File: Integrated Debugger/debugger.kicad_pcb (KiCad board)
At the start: 4 copper layers, 36.8 x 16.4 mm, 49 parts, among them J1 B2B GT-B0353FSV06-08B0201, J2 USB_C (PC <-> Host), J3 FPC socket 10P, J4 20021521-00010T1LF, J5 PWR, Q1 NMOS DMN2991UDA-7B, Q2 PMOS DMP32D9UDA-7B, SW1 RESET, SW2 BOOT, U1 TPS7A2633DRVR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

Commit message: feat: wip board layout and routing
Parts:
- C10, C11: moved to B.Cu
- D6, Q1, Q2, U1, U8: moved to F.Cu
- moved D6 65.4 mm to (104.4, 94.8), turned to -90 degrees
- moved Q2 63.2 mm to (105.9, 92.8)
- moved J1 62.8 mm to (129.9, 88.5), turned to 90 degrees
- moved U8 61.5 mm to (106.0, 95.2), turned to 0 degrees
- moved U1 56.8 mm to (123.0, 83.8), turned to -90 degrees
- moved R13 56.8 mm to (112.1, 94.1), turned to 90 degrees
- moved R14 54.4 mm to (113.2, 93.8)
- moved R15 53.5 mm to (113.2, 94.5), turned to 180 degrees
- moved C8 50.9 mm to (112.7, 84.3), turned to -90 degrees
- moved C3 48.9 mm to (120.6, 86.6), turned to 90 degrees
- moved R17 48.1 mm to (106.2, 91.6)
- moved C9 47.1 mm to (119.1, 85.0)
- moved R16 41.4 mm to (109.8, 83.9), turned to -90 degrees
- moved C10 32.4 mm to (110.0, 91.0)
- moved C13 31.3 mm to (108.6, 94.4)
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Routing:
- net V_TARGET: track 5.86 -> 29.8 mm, vias 1 -> 3
- net /MCU/~{RST}: track 0.00 -> 16.9 mm, vias 0 -> 2
- net /MCU/TARGET_EN: track 0.00 -> 15.2 mm, vias 0 -> 3
- net /MCU/SWD.IO: track 1.07 -> 15.4 mm
- net +5V: track 4.33 -> 18.1 mm
- net /Target/tRST: track 11.2 -> 22.9 mm, vias 1 -> 3
- net +3.3V: track 7.65 -> 18.6 mm, vias 1 -> 8
- net /MCU/TRACESWO: track 1.81 -> 12.4 mm
- net /MCU/SWD.CLK: track 2.67 -> 12.4 mm
- net /MCU/i.RX: track 16.6 -> 7.15 mm, vias 0 -> 2
- net /Target/tRXD: track 6.72 -> 14.8 mm
- net /Target Frontend/xRST: track 0.00 -> 7.73 mm
- net /MCU/i.RST_SEN: track 0.00 -> 7.67 mm, vias 0 -> 2
- net Net-(Q2-Pad1): track 0.00 -> 7.26 mm
- net /MCU/SOL_EN: track 0.00 -> 6.77 mm, vias 0 -> 1
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- added copper zone on B.Cu, net +3.3V
- added copper zone on F.Cu, net +3.3V

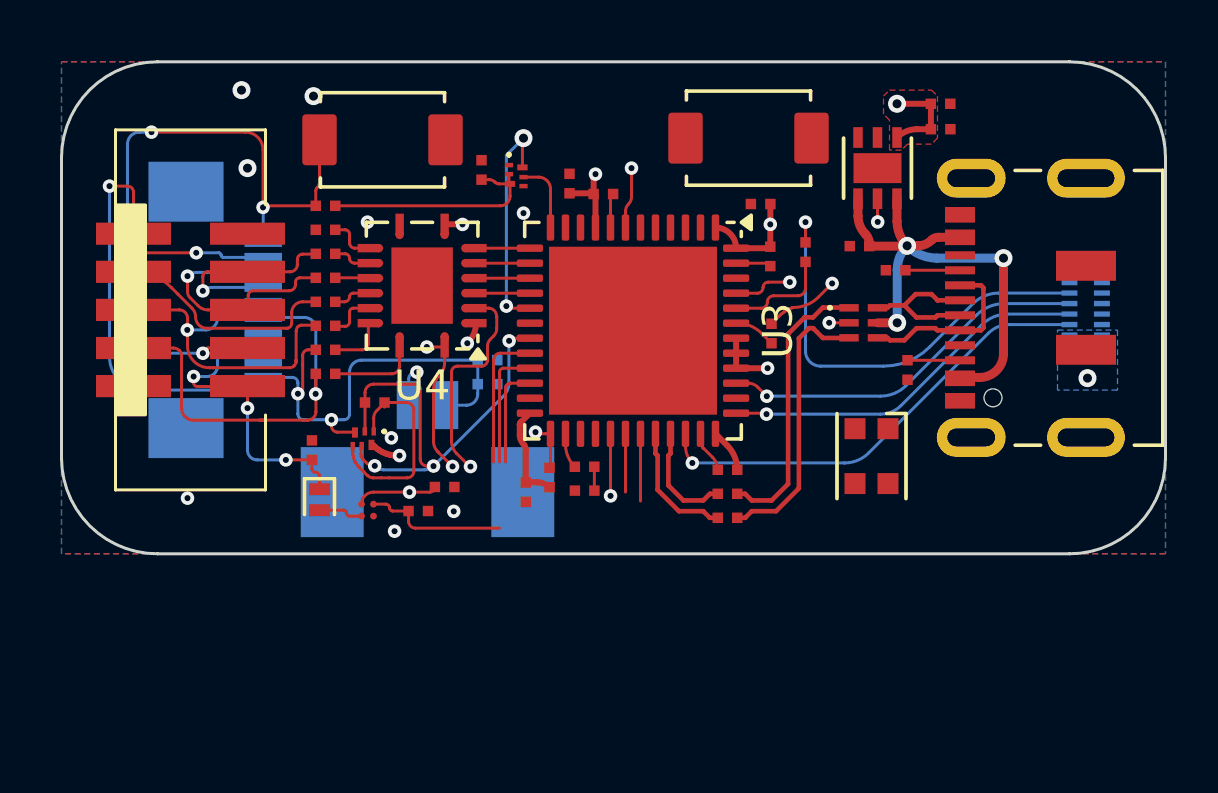
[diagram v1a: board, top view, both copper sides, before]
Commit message: feat: finish majority of routing
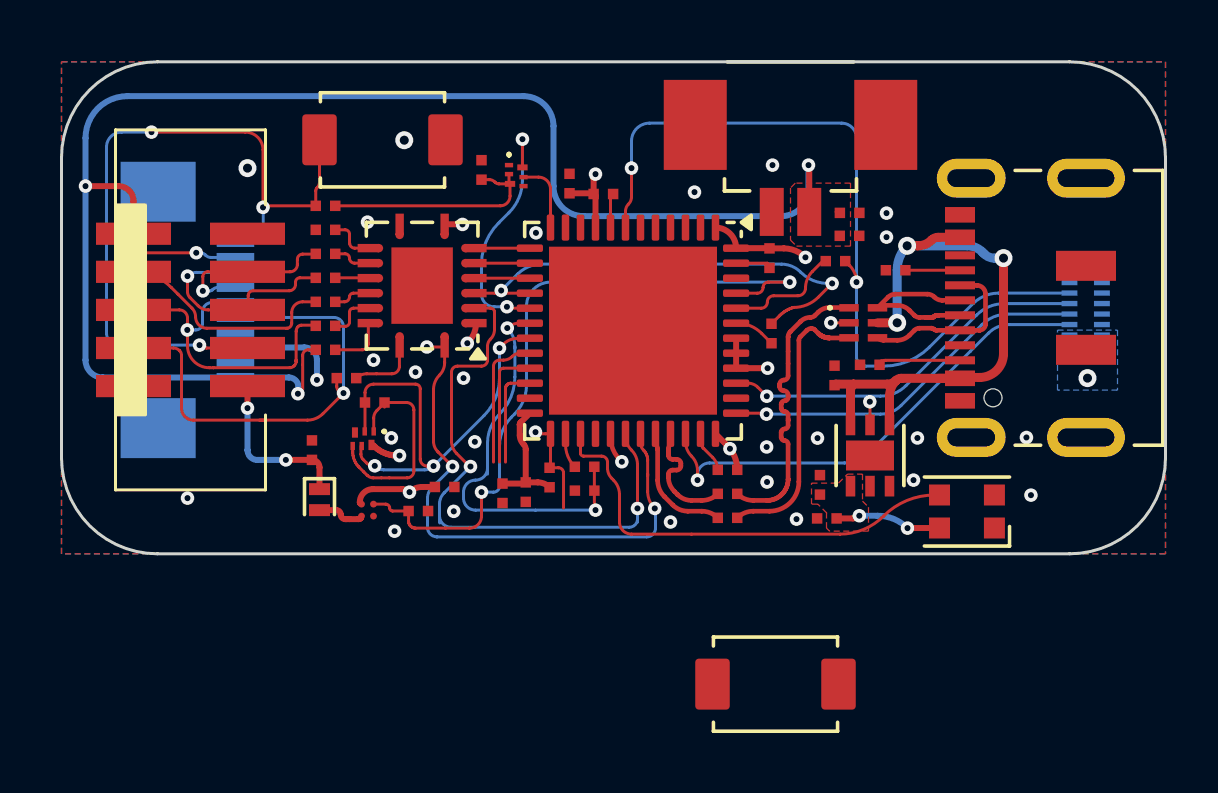
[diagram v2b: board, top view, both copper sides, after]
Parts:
- C10, C11, J5: moved to F.Cu
- moved SW2 18.2 mm to (119.6, 101.0)
- moved J5 17.2 mm to (120.1, 82.4)
- moved C12 14.3 mm to (121.3, 95.5), turned to 180 degrees
- moved C10 13.4 mm to (122.1, 85.3)
- moved C9 12.9 mm to (110.5, 94.6), turned to 90 degrees
- moved C11 12.8 mm to (122.1, 86.1)
- moved C2 12.5 mm to (121.1, 94.4), turned to 90 degrees
- moved U1 9.58 mm to (122.8, 93.4), turned to 90 degrees
- moved C1 4.39 mm to (121.6, 90.7), turned to 90 degrees
- moved D2 3.68 mm to (126.0, 95.2), turned to 180 degrees
- moved R11 1.27 mm to (122.7, 90.4), turned to 180 degrees
- moved C3 1.04 mm to (121.6, 86.9), turned to 0 degrees
- moved J3 0.93 mm to (100.4, 88.5)
- moved R6 0.71 mm to (105.3, 90.8)
- moved C6 0.06 mm to (119.4, 86.8)
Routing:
- net V_TARGET: track 29.8 -> 51.1 mm
- net /MCU/SOL_EN: track 6.77 -> 23.3 mm, vias 1 -> 2
- net /MCU/LEDX: track 0.32 -> 15.3 mm
- net Net-(U3-PB0): track 0.80 -> 13.5 mm, vias 0 -> 2
- net /MCU/i.RX: track 7.15 -> 18.8 mm, vias 2 -> 3
- net /MCU/i.TDO: track 4.28 -> 15.9 mm, vias 1 -> 2
- net /MCU/i.TX: track 9.14 -> 19.7 mm, vias 1 -> 2
- net /MCU/~{RST}: track 16.9 -> 27.2 mm
- net +5V: track 18.1 -> 21.6 mm
- net /Target/tRXD: track 14.8 -> 17.1 mm
- net V_SOLAR: track 11.7 -> 9.58 mm
- net /Target/tRST: track 22.9 -> 24.9 mm
- net Net-(SW2-B): track 1.65 -> 3.38 mm
- net /D+: track 5.08 -> 6.46 mm
- net GND: track 7.25 -> 5.92 mm, vias 12 -> 27
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- added copper zone on F.Cu, net V_TARGET
